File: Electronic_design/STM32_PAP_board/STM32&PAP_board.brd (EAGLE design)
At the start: 100 x 80 mm, 21 parts

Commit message: modification regulateur 3V3
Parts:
- removed 3.3V: (no value), v-reg:TO220S
- added 3V3: 7805T, linear:TO220H
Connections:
- net GND: now also 3V3.2; no longer 3.3V.1
- net N$41: now also 3V3.3; no longer 3.3V.2
- net N$42: now also 3V3.1; no longer 3.3V.3
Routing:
- net N$42: track 27.8 -> 64.6 mm
- net N$41: track 16.7 -> 12.6 mm
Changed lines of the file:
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@@
 <text x="16.129" y="66.929" size="1.778" layer="27" font="vector" rot="R90">GND</text>
 <text x="18.796" y="68.453" size="1.778" layer="27" font="vector" rot="R90">3V</text>
-<text x="36.068" y="70.358" size="1.778" layer="27" font="vector">GND</text>
-<text x="35.941" y="72.644" size="1.778" layer="27" font="vector">3V</text>
+<text x="30.861" y="66.167" size="1.778" layer="27" font="vector" rot="R270">GND</text>
+<text x="33.909" y="66.167" size="1.778" layer="27" font="vector" rot="R270">3V</text>
 <text x="8.382" y="69.342" size="1.778" layer="25" font="vector" rot="R90">VIN</text>
-<text x="38.989" y="76.835" size="1.778" layer="25" font="vector" rot="R180">VIN</text>
+<text x="27.686" y="66.167" size="1.778" layer="25" font="vector" rot="R270">VIN</text>
 <text x="81.28" y="40.64" size="1.778" layer="25" font="vector" rot="R270">MOTOR1</text>
 <text x="81.28" y="17.78" size="1.778" layer="25" font="vector" rot="R270">MOTOR2</text>
@@
 <attribute name="OC_NEWARK" value="unknown" x="27.94" y="26.67" size="1.778" layer="27" rot="R270" display="off"/>
 </element>
-<element name="3.3V" library="v-reg" package="TO220S" value="" x="30.226" y="73.66" rot="R90"/>
 <element name="SV4" library="con-lstb" package="MA04-1" value="" x="91.44" y="36.83" rot="R270">
 <attribute name="MF" value="" x="91.44" y="36.83" size="1.778" layer="27" rot="R270" display="off"/>
@@
 <attribute name="OC_NEWARK" value="unknown" x="4.62" y="60.06" size="1.778" layer="27" rot="R270" display="off"/>
 </element>
+<element name="3V3" library="linear" library_urn="urn:adsk.eagle:library:262" package="TO220H" package3d_urn="urn:adsk.eagle:package:16414/1" value="7805T" x="31.308" y="80.969"/>
 </elements>
 <signals>
@@
 </signal>
 <signal name="GND">
-<contactref element="3.3V" pad="1"/>
 <contactref element="U$3" pad="P$19"/>
 <contactref element="SV2" pad="2"/>
@@
 </polygon>
 <contactref element="SL1" pad="3"/>
+<contactref element="3V3" pad="2"/>
 </signal>
 <signal name="N$43">
@@
 <contactref element="U$2" pad="GND1"/>
 </signal>
-<signal name="N$41">
-<contactref element="3.3V" pad="2"/>
-<wire x1="45.72" y1="73.7616" x2="32.766" y2="73.7616" width="0.5" layer="1"/>
-<wire x1="32.766" y1="73.7616" x2="32.766" y2="73.66" width="0.1524" layer="1"/>
-<contactref element="F1" pad="1"/>
-<wire x1="45.72" y1="73.7616" x2="46.2" y2="73.2816" width="0.5" layer="1"/>
-<wire x1="46.2" y1="73.2816" x2="46.2" y2="70.3" width="0.5" layer="1"/>
-</signal>
 <signal name="N$42">
 <contactref element="U$4" pad="P$2"/>
 <contactref element="SV1" pad="3"/>
-<contactref element="3.3V" pad="3"/>
 <wire x1="7.7724" y1="76.2" x2="7.747" y2="76.2" width="0.1524" layer="1"/>
-<wire x1="32.895" y1="76.071" x2="60.706" y2="76.071" width="2.54" layer="1"/>
-<wire x1="32.895" y1="76.071" x2="32.766" y2="76.2" width="0" layer="19" extent="1-1"/>
-<wire x1="7.7724" y1="76.2" x2="32.766" y2="76.2" width="0" layer="19" extent="1-1"/>
+<contactref element="3V3" pad="1"/>
+<wire x1="29.871" y1="76.071" x2="60.706" y2="76.071" width="2.54" layer="1"/>
+<wire x1="28.768" y1="70.809" x2="28.768" y2="74.968" width="2.54" layer="1"/>
+<wire x1="28.768" y1="74.968" x2="29.871" y2="76.071" width="2.54" layer="1"/>
+<wire x1="7.747" y1="76.2" x2="7.747" y2="72.333" width="2.54" layer="1"/>
+<wire x1="7.747" y1="72.333" x2="12.32" y2="67.76" width="2.54" layer="1"/>
+<wire x1="12.32" y1="67.76" x2="25.719" y2="67.76" width="2.54" layer="1"/>
+<wire x1="25.719" y1="67.76" x2="28.768" y2="70.809" width="2.54" layer="1"/>
 </signal>
 <signal name="N$1">
@@
 <contactref element="U$2" pad="GND2"/>
 </signal>
+<signal name="N$41">
+<contactref element="3V3" pad="3"/>
+<contactref element="F1" pad="1"/>
+<wire x1="33.848" y1="70.809" x2="45.691" y2="70.809" width="0.508" layer="1"/>
+<wire x1="45.691" y1="70.809" x2="46.2" y2="70.3" width="0.508" layer="1"/>
+</signal>
 </signals>
 </board>
 </drawing>
+<compatibility>
+<note version="8.2" severity="warning">
+Since Version 8.2, EAGLE supports online libraries. The ids
+of those online libraries will not be understood (or retained)
+with this version.
+</note>
+<note version="8.3" severity="warning">
+Since Version 8.3, EAGLE supports URNs for individual library
+assets (packages, symbols, and devices). The URNs of those assets
+will not be understood (or retained) with this version.
+</note>
+<note version="8.3" severity="warning">
+Since Version 8.3, EAGLE supports the association of 3D packages
+with devices in libraries, schematics, and board files. Those 3D
+packages will not be understood (or retained) with this version.
+</note>
+</compatibility>
 </eagle>

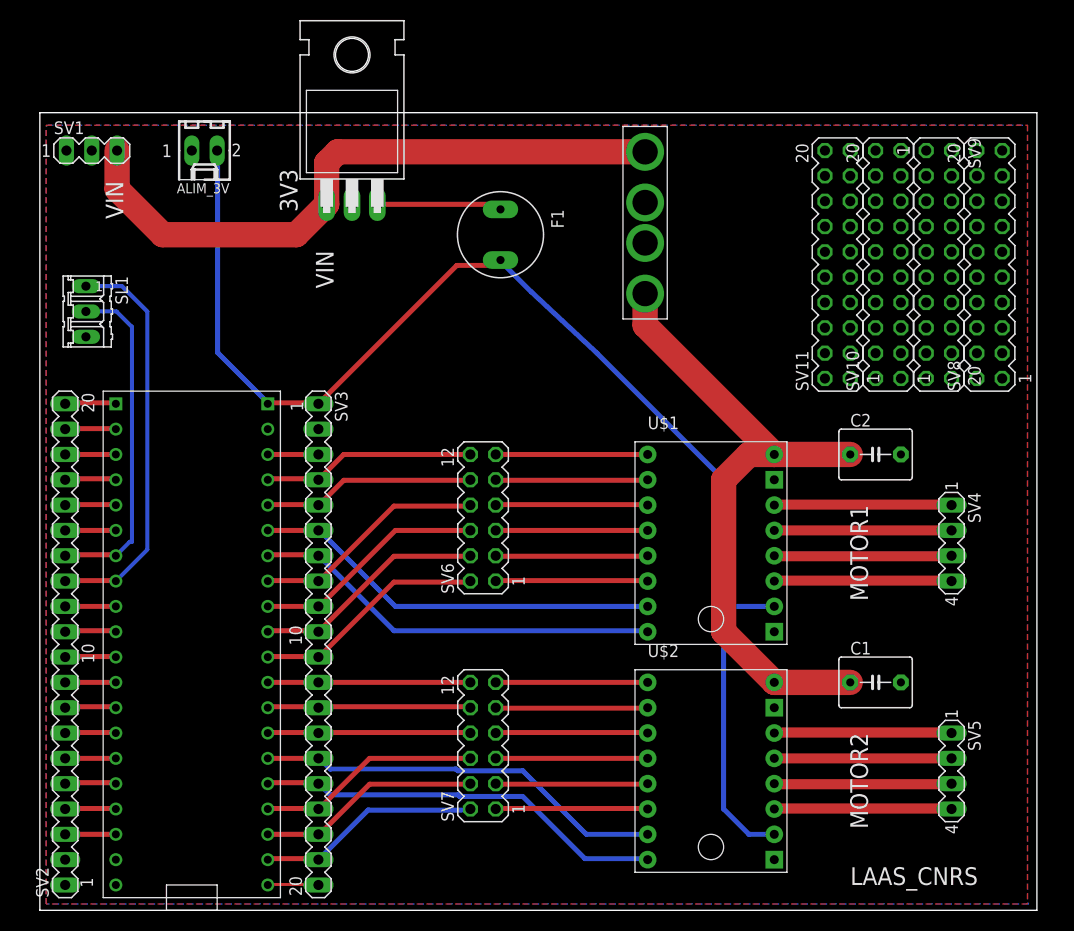
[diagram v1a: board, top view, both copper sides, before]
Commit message: ajout connecteur vert et trous de fixation
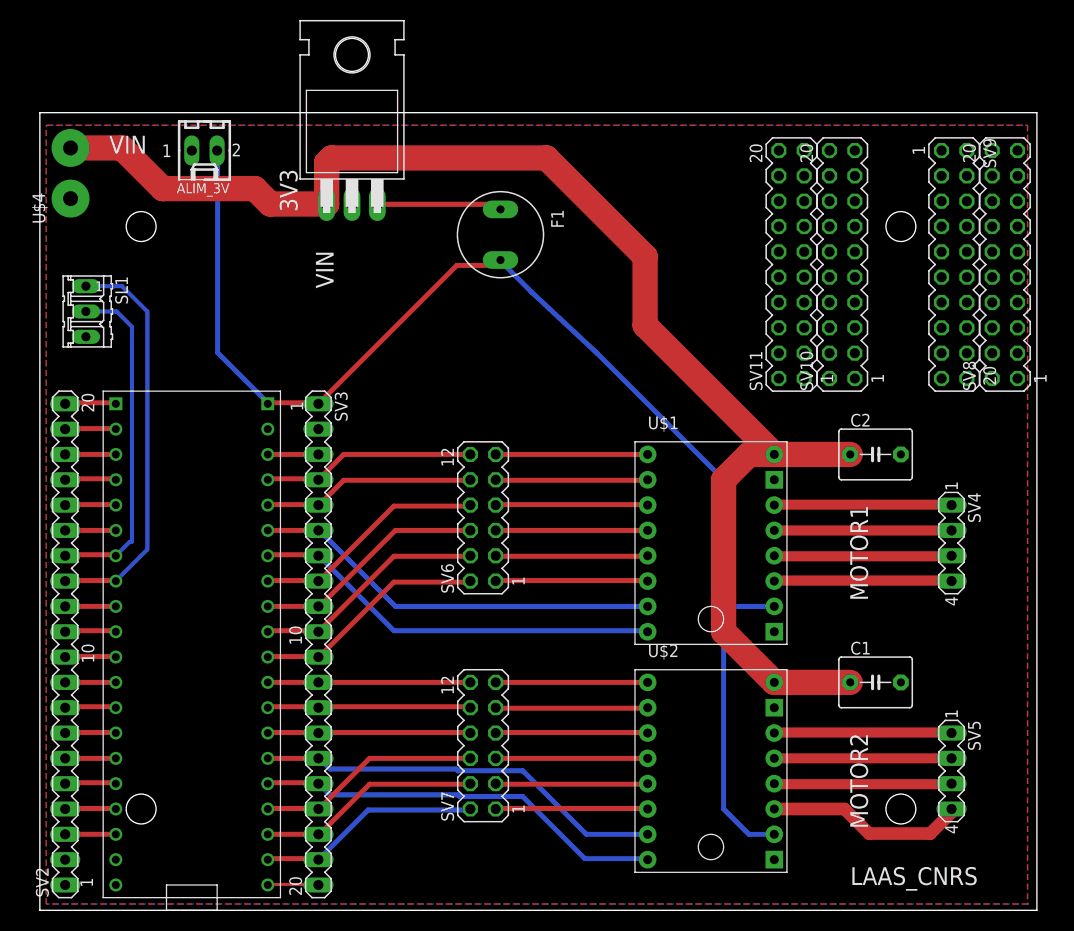
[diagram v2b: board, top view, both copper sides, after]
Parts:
- removed SV1: (no value), con-lstb:MA03-1
- added U$5: (no value), Trous_fixation:TROUS_FIXATION
- U$4: value AUTO_FUSE -> GREEN_HEADER; device AUTO_FUSE:AUTO_FUSE -> PowerHeaders:GREEN_HEADER
- moved U$4 57.8 mm to (3.08, 73.9), turned to 90 degrees
- moved SV10 4.62 mm to (80.5, 64.8)
- moved SV11 4.62 mm to (75.4, 64.8)
- moved SV8 1.54 mm to (96.8, 64.8)
- moved SV9 1.54 mm to (91.7, 64.8)
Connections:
- removed net N$43: C1.1, C2.1, U$1.VMOT, U$2.VMOT, U$4.P$4
- net GND: now also U$4.P$1; no longer SV1.1
- net N$42: now also C1.1, C2.1, U$1.VMOT, U$2.VMOT; no longer SV1.3
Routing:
- net N$42: track 64.6 -> 137.4 mm
- net N$43: track 65.3 -> 0.00 mm
- net N$44: track 17.8 -> 20.2 mm

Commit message: ameliorations
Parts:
- added SV1: (no value), con-lstb:MA10-1
- SV2: device con-lstb:MA20-1 -> con-lstb:MA08-1
- moved SV2 10.2 mm to (2.59, 16.5)
- moved SV10 1.54 mm to (82.0, 64.8)
- moved SV11 1.54 mm to (76.9, 64.8)
- moved U$4 0.64 mm to (2.44, 73.9)
- renumbered SL1 to UART2
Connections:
- net GND: no longer SV2.1, SV2.2
- net N$10: now also SV2.8; no longer SV2.10
- net N$11: now also SV1.1; no longer SV2.11
- net N$12: now also SV1.2; no longer SV2.12
- net N$13: now also SV1.3, UART2.2; no longer SV2.13, UART2.1
- net N$14: now also SV1.4, UART2.1; no longer SV2.14, UART2.2
- net N$15: now also SV1.5; no longer SV2.15
- net N$16: now also SV1.6; no longer SV2.16
- net N$17: now also SV1.7; no longer SV2.17
- net N$18: now also SV1.8; no longer SV2.18
- net N$19: now also SV1.9; no longer SV2.19
- net N$20: now also SV1.10; no longer SV2.20
- net N$3: now also SV2.1; no longer SV2.3
- net N$4: now also SV2.2; no longer SV2.4
- net N$5: now also SV2.3; no longer SV2.5
- net N$6: now also SV2.4; no longer SV2.6
- net N$7: now also SV2.5; no longer SV2.7
- net N$8: now also SV2.6; no longer SV2.8
- net N$9: now also SV2.7; no longer SV2.9
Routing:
- net N$44: track 20.2 -> 17.9 mm
- net N$13: track 40.7 -> 39.7 mm
- net N$14: track 34.3 -> 35.3 mm
- net N$42: track 137.4 -> 138.1 mm
- net GND: track 0.61 -> 0.00 mm

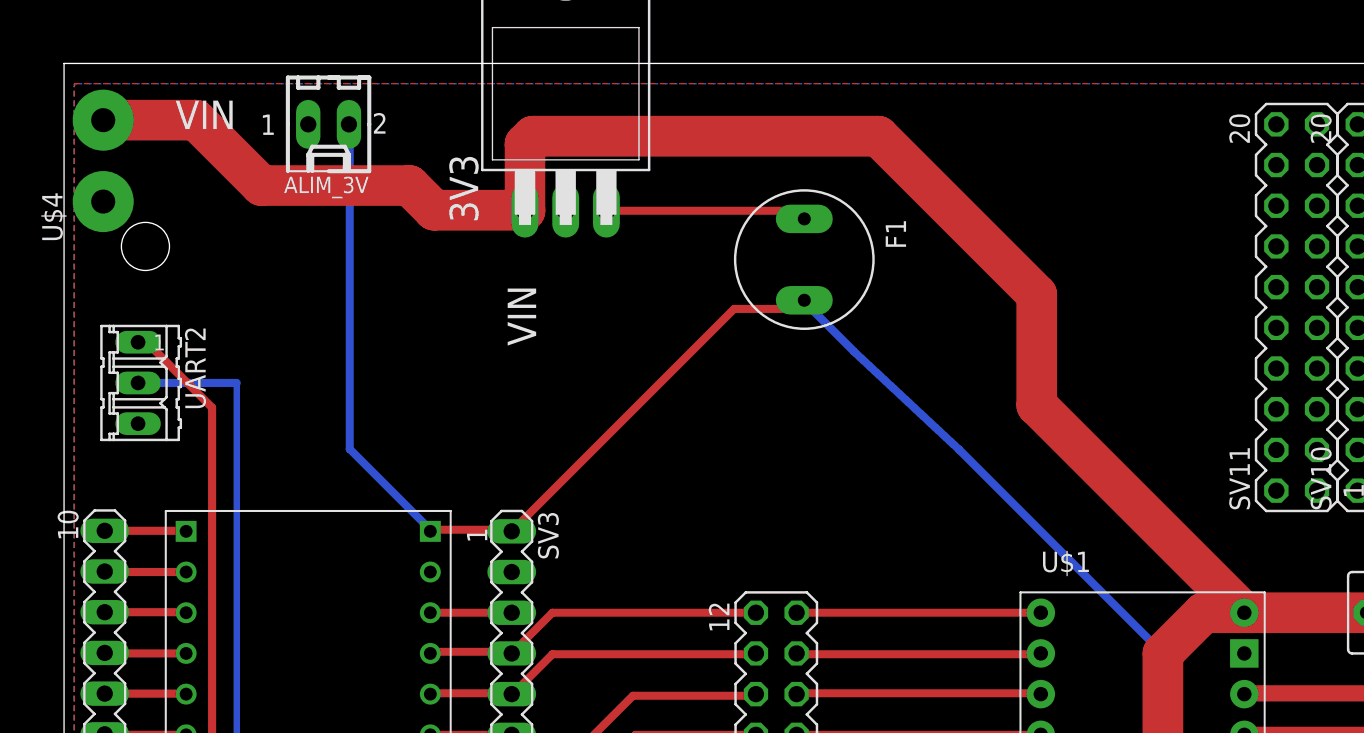
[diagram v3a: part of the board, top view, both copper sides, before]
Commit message: elargissement pistes
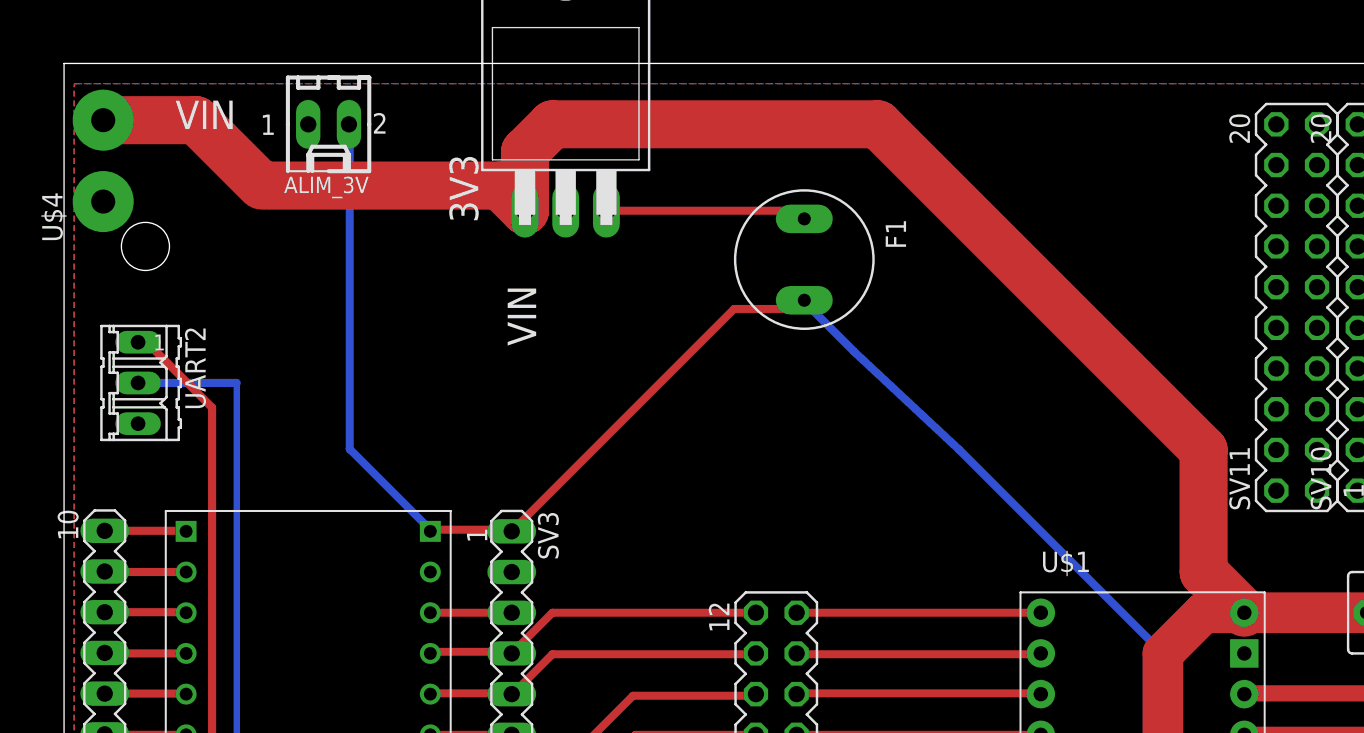
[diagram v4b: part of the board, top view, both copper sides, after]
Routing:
- net N$42: track 138.1 -> 138.8 mm
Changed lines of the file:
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@@
 <layer number="42" name="bRestrict" color="1" fill="10" visible="yes" active="yes"/>
 <layer number="43" name="vRestrict" color="2" fill="10" visible="yes" active="yes"/>
-<layer number="44" name="Drills" color="7" fill="1" visible="no" active="yes"/>
+<layer number="44" name="Drills" color="7" fill="1" visible="yes" active="yes"/>
 <layer number="45" name="Holes" color="7" fill="1" visible="no" active="yes"/>
 <layer number="46" name="Milling" color="3" fill="1" visible="no" active="yes"/>
@@
 <wire x1="68.58" y1="43.18" x2="68.58" y2="27.94" width="2.54" layer="1"/>
 <wire x1="73.66" y1="22.86" x2="68.58" y2="27.94" width="2.54" layer="1"/>
-<wire x1="73.66" y1="45.72" x2="60.706" y2="58.674" width="2.54" layer="1"/>
+<wire x1="73.6586" y1="45.7214" x2="73.66" y2="45.72" width="2.54" layer="1"/>
 <wire x1="73.66" y1="45.72" x2="81.28" y2="45.72" width="2.54" layer="1"/>
 <wire x1="81.28" y1="22.86" x2="73.66" y2="22.86" width="2.54" layer="1"/>
 <contactref element="U$4" pad="P$2"/>
-<wire x1="2.445" y1="76.46" x2="8.24" y2="76.46" width="2.54" layer="1"/>
-<wire x1="8.24" y1="76.46" x2="12.32" y2="72.38" width="2.54" layer="1"/>
-<wire x1="12.32" y1="72.38" x2="21.56" y2="72.38" width="2.54" layer="1"/>
-<wire x1="21.56" y1="72.38" x2="23.1" y2="70.84" width="2.54" layer="1"/>
-<wire x1="28.737" y1="70.84" x2="23.1" y2="70.84" width="2.54" layer="1"/>
-<wire x1="28.737" y1="70.84" x2="28.768" y2="70.809" width="2.54" layer="1"/>
-<wire x1="60.706" y1="58.674" x2="60.706" y2="65.574" width="2.54" layer="1"/>
-<wire x1="50.82" y1="75.46" x2="60.706" y2="65.574" width="2.54" layer="1"/>
-<wire x1="28.768" y1="70.809" x2="28.768" y2="74.968" width="2.54" layer="1"/>
-<wire x1="28.768" y1="74.968" x2="29.26" y2="75.46" width="2.54" layer="1"/>
-<wire x1="29.26" y1="75.46" x2="50.82" y2="75.46" width="2.54" layer="1"/>
+<wire x1="12.32" y1="72.38" x2="12.7" y2="72.38" width="2.54" layer="1"/>
+<wire x1="28.768" y1="70.809" x2="28.768" y2="74.488" width="3" layer="1"/>
+<wire x1="28.768" y1="74.488" x2="30.48" y2="76.2" width="3" layer="1"/>
+<wire x1="30.48" y1="76.2" x2="50.8" y2="76.2" width="3" layer="1"/>
+<wire x1="71.12" y1="55.88" x2="71.12" y2="48.26" width="3" layer="1"/>
+<wire x1="71.12" y1="48.26" x2="73.6586" y2="45.7214" width="3" layer="1"/>
+<wire x1="50.8" y1="76.2" x2="71.12" y2="55.88" width="3" layer="1"/>
+<wire x1="2.445" y1="76.46" x2="8.24" y2="76.46" width="3" layer="1"/>
+<wire x1="8.24" y1="76.46" x2="12.32" y2="72.38" width="3" layer="1"/>
+<wire x1="27.197" y1="72.38" x2="28.768" y2="70.809" width="3" layer="1"/>
+<wire x1="12.7" y1="72.38" x2="27.197" y2="72.38" width="3" layer="1"/>
 </signal>
 <signal name="N$1">

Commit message: ajout condensateurs
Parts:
- added C3: (no value), rcl:E5-13
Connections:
- net GND: now also C3.-
- net N$42: now also C3.+
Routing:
- net N$42: track 138.8 -> 143.9 mm
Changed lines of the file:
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@@
 <attribute name="OC_NEWARK" value="unknown" x="4.62" y="60.06" size="1.778" layer="27" rot="R270" display="off"/>
 </element>
-<element name="3V3" library="linear" library_urn="urn:adsk.eagle:library:262" package="TO220H" package3d_urn="urn:adsk.eagle:package:16414/1" value="7805T" x="31.308" y="80.969"/>
+<element name="3V3" library="linear" library_urn="urn:adsk.eagle:library:262" package="TO220H" package3d_urn="urn:adsk.eagle:package:16414/1" value="7805T" x="31.308" y="80.969" smashed="yes"/>
 <element name="U$4" library="PowerHeaders" package="GREEN_HEADER" value="GREEN_HEADER" x="2.445" y="73.92" rot="R90"/>
 <element name="U$5" library="Trous_fixation" package="TROUS_FIXATION" value="" x="0" y="0"/>
@@
 <attribute name="OC_NEWARK" value="unknown" x="2.59" y="16.51" size="1.778" layer="27" rot="R90" display="off"/>
 </element>
+<element name="C3" library="rcl" library_urn="urn:adsk.eagle:library:334" package="E5-13" package3d_urn="urn:adsk.eagle:package:23375/1" value="" x="66.04" y="71.12" rot="R90"/>
 </elements>
 <signals>
@@
 <contactref element="U$4" pad="P$1"/>
 <contactref element="UART2" pad="3"/>
+<contactref element="C3" pad="-"/>
 </signal>
 <signal name="N$45">
@@
 <wire x1="68.58" y1="43.18" x2="68.58" y2="27.94" width="2.54" layer="1"/>
 <wire x1="73.66" y1="22.86" x2="68.58" y2="27.94" width="2.54" layer="1"/>
-<wire x1="73.6586" y1="45.7214" x2="73.66" y2="45.72" width="2.54" layer="1"/>
 <wire x1="73.66" y1="45.72" x2="81.28" y2="45.72" width="2.54" layer="1"/>
 <wire x1="81.28" y1="22.86" x2="73.66" y2="22.86" width="2.54" layer="1"/>
 <contactref element="U$4" pad="P$2"/>
 <wire x1="12.32" y1="72.38" x2="12.7" y2="72.38" width="2.54" layer="1"/>
-<wire x1="28.768" y1="70.809" x2="28.768" y2="74.488" width="3" layer="1"/>
-<wire x1="28.768" y1="74.488" x2="30.48" y2="76.2" width="3" layer="1"/>
-<wire x1="30.48" y1="76.2" x2="50.8" y2="76.2" width="3" layer="1"/>
-<wire x1="71.12" y1="55.88" x2="71.12" y2="48.26" width="3" layer="1"/>
-<wire x1="71.12" y1="48.26" x2="73.6586" y2="45.7214" width="3" layer="1"/>
-<wire x1="50.8" y1="76.2" x2="71.12" y2="55.88" width="3" layer="1"/>
 <wire x1="2.445" y1="76.46" x2="8.24" y2="76.46" width="3" layer="1"/>
 <wire x1="8.24" y1="76.46" x2="12.32" y2="72.38" width="3" layer="1"/>
 <wire x1="27.197" y1="72.38" x2="28.768" y2="70.809" width="3" layer="1"/>
 <wire x1="12.7" y1="72.38" x2="27.197" y2="72.38" width="3" layer="1"/>
+<contactref element="C3" pad="+"/>
+<wire x1="28.768" y1="70.809" x2="28.768" y2="74.488" width="3" layer="1"/>
+<wire x1="28.768" y1="74.488" x2="30.48" y2="76.2" width="3" layer="1"/>
+<wire x1="30.48" y1="76.2" x2="50.8" y2="76.2" width="3" layer="1"/>
+<wire x1="50.8" y1="76.2" x2="60.96" y2="66.04" width="3" layer="1"/>
+<wire x1="63.5" y1="66.04" x2="60.96" y2="66.04" width="3" layer="1"/>
+<wire x1="63.5" y1="66.04" x2="66.04" y2="68.58" width="3" layer="1"/>
+<wire x1="73.66" y1="45.72" x2="71.12" y2="48.26" width="2.54" layer="1"/>
+<wire x1="71.12" y1="48.26" x2="71.12" y2="55.88" width="3" layer="1"/>
+<wire x1="71.12" y1="55.88" x2="63.5" y2="63.5" width="3" layer="1"/>
+<wire x1="63.5" y1="63.5" x2="63.5" y2="66.04" width="3" layer="1"/>
 </signal>
 <signal name="N$1">
@@
 <wire x1="17.8308" y1="76.2" x2="17.78" y2="76.2" width="0.1524" layer="16"/>
 <wire x1="22.86" y1="50.9016" x2="22.86" y2="50.8" width="0.1524" layer="16"/>
-<wire x1="27.94" y1="50.8" x2="41.82" y2="64.68" width="0.5" layer="1"/>
+<wire x1="27.94" y1="50.8" x2="41.82" y2="64.68" width="1.016" layer="1"/>
 <contactref element="U$2" pad="VDD"/>
 <contactref element="U$1" pad="VDD"/>
@@
 <wire x1="49.278" y1="62.04" x2="46.2" y2="65.118" width="0.5" layer="16"/>
 <wire x1="46.2" y1="65.118" x2="46.2" y2="65.22" width="0.5" layer="16"/>
-<wire x1="41.82" y1="64.68" x2="46.2" y2="64.68" width="0.5" layer="1"/>
+<wire x1="41.82" y1="64.68" x2="46.2" y2="64.68" width="1.016" layer="1"/>
 <wire x1="46.2" y1="64.68" x2="46.2" y2="65.22" width="0.5" layer="1"/>
 </signal>
@@
 <contactref element="3V3" pad="3"/>
 <contactref element="F1" pad="1"/>
-<wire x1="33.848" y1="70.809" x2="45.691" y2="70.809" width="0.508" layer="1"/>
+<wire x1="33.848" y1="70.809" x2="45.691" y2="70.809" width="1.016" layer="1"/>
 <wire x1="45.691" y1="70.809" x2="46.2" y2="70.3" width="0.508" layer="1"/>
 </signal>
